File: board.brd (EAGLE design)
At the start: 26.3 x 33.6 mm, 46 parts, among them IC1 ATMEGA48/88/168-AU, IC2 TP4056, IC3 MAX31865, Q1 PH2925U, Q2 IRLML2244, U1 LM3480-3.3

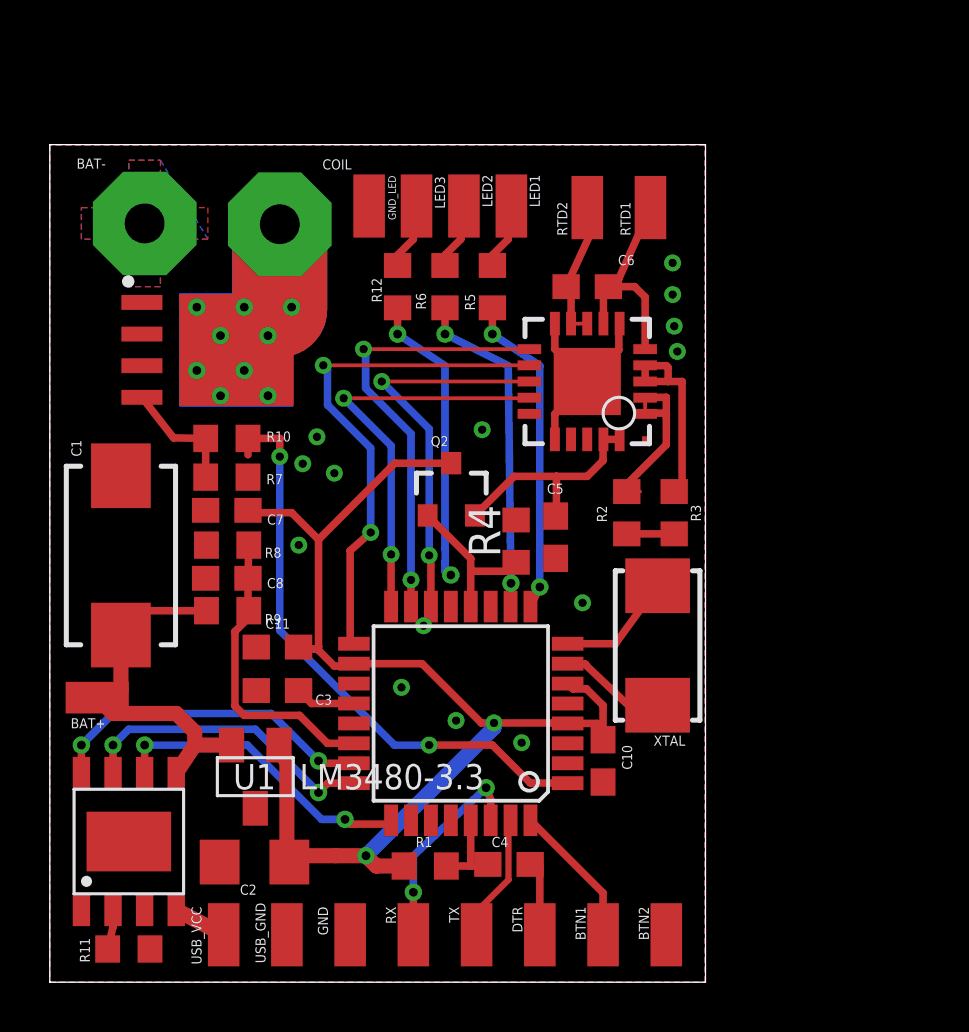
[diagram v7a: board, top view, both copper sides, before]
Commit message: rearanging led and spi traces, adding vias for gnd and heat, checking layout, READY for production
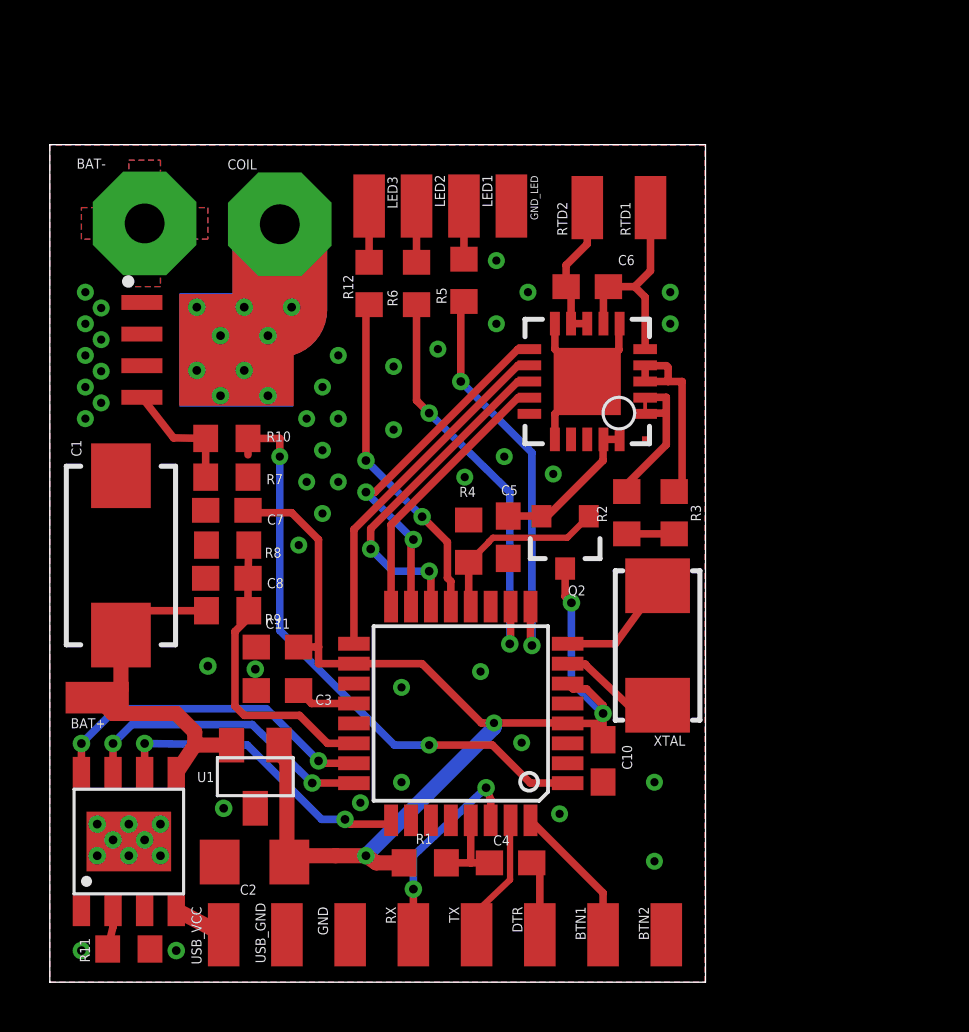
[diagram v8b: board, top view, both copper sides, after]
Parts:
- moved GND_LED 5.72 mm to (18.5, 31.2)
- moved Q2 5.00 mm to (20.7, 17.7), turned to 180 degrees
- moved C5 1.91 mm to (18.4, 17.9)
- moved LED1 1.91 mm to (16.6, 31.2)
- moved LED2 1.91 mm to (14.7, 31.2)
- moved R4 1.91 mm to (16.8, 17.7)
- moved LED3 1.90 mm to (12.8, 31.2)
- moved R5 1.17 mm to (16.6, 28.2)
- moved R12 1.15 mm to (12.8, 28.1)
- moved R6 1.15 mm to (14.7, 28.1)
- moved R1 0.13 mm to (15.1, 4.79)
- moved C4 0.09 mm to (18.5, 4.79)
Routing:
- net D13_SCK: track 20.7 -> 14.4 mm, vias 2 -> 0
- net D12_MISO: track 16.6 -> 11.0 mm, vias 2 -> 0
- net D5_LED1: track 13.1 -> 16.6 mm
- net D11_MOSI: track 17.8 -> 14.4 mm
- net D6_LED2: track 13.8 -> 16.8 mm
- net VCC_MAX: track 9.19 -> 6.25 mm
- net D10_CS: track 15.8 -> 13.8 mm
- net D9_LED3: track 11.9 -> 13.6 mm
- net D8_VCC_MAX: track 6.35 -> 7.46 mm
- net TEMP_REF+: track 7.40 -> 6.35 mm
- net LED1: track 2.70 -> 2.13 mm
- net VCC: track 48.7 -> 48.8 mm, vias 2 -> 4
- net GND: vias 14 -> 50
